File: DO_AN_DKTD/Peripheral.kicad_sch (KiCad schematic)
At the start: 92 parts, among them IC1 RTC_DS3231M, J1 Conn_01x03, J2 Conn_01x02, J4 Conn_01x04, J5 Conn_01x02, J8 Micro_SD_Card_Det1, J9 USB_C_Receptacle, Q1 NPN, Q2 NPN, Q3 NPN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

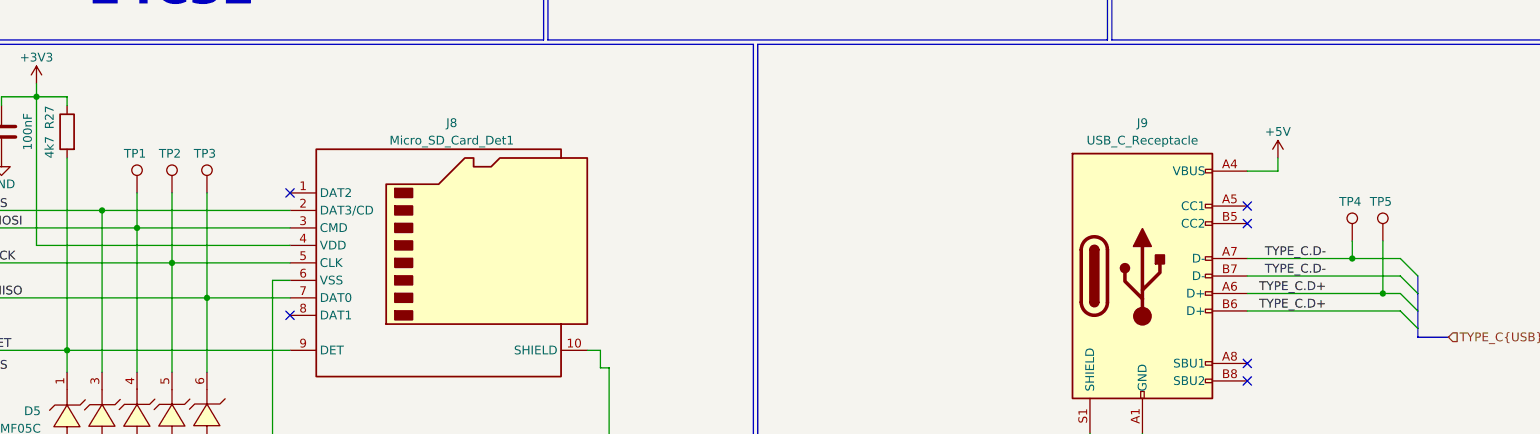
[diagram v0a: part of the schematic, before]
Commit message: add testoint SPI USB LEDTEST and Buck power
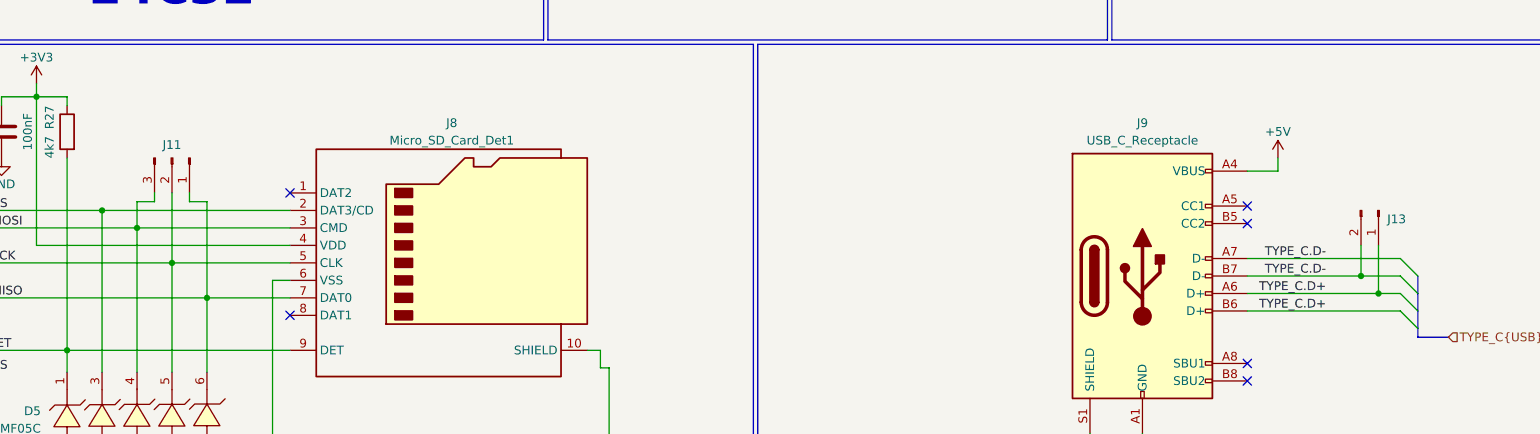
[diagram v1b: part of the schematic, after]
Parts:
- removed TP1, TP2, TP3, TP4, TP5: TestPoint, TestPoint:TestPoint_THTPad_D2.0mm_Drill1.0mm, symbol Connector:TestPoint
- added J11: Conn_01x03_Pin, Connector_PinHeader_2.00mm:PinHeader_1x03_P2.00mm_Vertical, symbol Connector:Conn_01x03_Pin
- added J13: Conn_01x02_Pin, Connector_PinHeader_2.00mm:PinHeader_1x02_P2.00mm_Vertical, symbol Connector:Conn_01x02_Pin
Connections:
- net SD.MISO: now also J11.1 (Pin_1)
- net SD.MOSI: now also J11.3 (Pin_3)
- net SD.SCK: now also J11.2 (Pin_2)
- net TYPE_C.D+: now also J13.1 (Pin_1)
- net TYPE_C.D-: now also J13.2 (Pin_2)

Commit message: commit to change branch
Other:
- note added: "BUZZER"
- note added: "USB TYPE-C"
- moved on the sheet: BZ1, Q9, R27
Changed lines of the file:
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@@
   )
   (bus_alias "pLORA" (members "INT" "CS" "RST"))
-  (bus_alias "SPI" (members "SCK" "MOSI" "MISO"))
   (bus_alias "I2C" (members "SDA" "SCL"))
+  (bus_alias "SPI" (members "SCK" "MOSI" "MISO"))
   (junction (at 258.445 239.395) (diameter 0) (color 0 0 0 0)
   )
@@
   (junction (at 132.715 130.175) (diameter 0) (color 0 0 0 0)
   )
-  (junction (at 376.555 214.63) (diameter 0) (color 0 0 0 0)
+  (junction (at 422.91 238.76) (diameter 0) (color 0 0 0 0)
   )
   (junction (at 247.015 186.055) (diameter 0) (color 0 0 0 0)
@@
   (junction (at 136.525 122.555) (diameter 0) (color 0 0 0 0)
   )
-  (junction (at 367.03 203.835) (diameter 0) (color 0 0 0 0)
+  (junction (at 413.385 227.965) (diameter 0) (color 0 0 0 0)
   )
   (junction (at 347.345 74.295) (diameter 0) (color 0 0 0 0)
@@
     (stroke (width 0) (type default))
   )
+  (polyline (pts (xy 354.33 176.53) (xy 354.33 281.305))
+    (stroke (width 0) (type default))
+  )
   (polyline (pts (xy 354.33 95.25) (xy 486.41 95.25))
     (stroke (width 0) (type default))
@@
     (stroke (width 0) (type default))
   )
-  (wire (pts (xy 367.03 213.36) (xy 367.03 214.63))
+  (wire (pts (xy 413.385 237.49) (xy 413.385 238.76))
     (stroke (width 0) (type default))
   )
@@
     (stroke (width 0) (type default))
   )
+  (polyline (pts (xy 354.33 176.53) (xy 486.41 176.53))
+    (stroke (width 0) (type default))
+  )
   (polyline (pts (xy 217.17 95.25) (xy 353.695 95.25))
     (stroke (width 0) (type default))
@@
     (stroke (width 0) (type default))
   )
+  (polyline (pts (xy 486.41 176.53) (xy 486.41 281.305))
+    (stroke (width 0) (type default))
+  )
   (bus (pts (xy 123.825 60.96) (xy 131.445 60.96))
     (stroke (width 0) (type default))
@@
     (stroke (width 0) (type default))
   )
-  (wire (pts (xy 364.49 203.835) (xy 367.03 203.835))
+  (wire (pts (xy 410.845 227.965) (xy 413.385 227.965))
     (stroke (width 0) (type default))
   )
@@
     (stroke (width 0) (type default))
   )
-  (wire (pts (xy 377.19 194.945) (xy 376.555 194.945))
+  (wire (pts (xy 423.545 219.075) (xy 422.91 219.075))
     (stroke (width 0) (type default))
   )
@@
     (stroke (width 0) (type default))
   )
-  (wire (pts (xy 367.03 205.74) (xy 367.03 203.835))
+  (wire (pts (xy 413.385 229.87) (xy 413.385 227.965))
     (stroke (width 0) (type default))
   )
@@
     (stroke (width 0) (type default))
   )
-  (wire (pts (xy 367.03 214.63) (xy 376.555 214.63))
+  (wire (pts (xy 413.385 238.76) (xy 422.91 238.76))
     (stroke (width 0) (type default))
   )
@@
     (stroke (width 0) (type default))
   )
-  (wire (pts (xy 367.03 203.835) (xy 368.935 203.835))
+  (wire (pts (xy 413.385 227.965) (xy 415.29 227.965))
     (stroke (width 0) (type default))
   )
@@
     (stroke (width 0) (type default))
   )
-  (wire (pts (xy 377.19 189.865) (xy 376.555 189.865))
+  (wire (pts (xy 423.545 213.995) (xy 422.91 213.995))
     (stroke (width 0) (type default))
   )
@@
     (stroke (width 0) (type default))
   )
-  (wire (pts (xy 376.555 208.915) (xy 376.555 214.63))
+  (wire (pts (xy 422.91 233.045) (xy 422.91 238.76))
     (stroke (width 0) (type default))
   )
@@
     (stroke (width 0) (type default))
   )
-  (wire (pts (xy 376.555 194.945) (xy 376.555 198.755))
+  (wire (pts (xy 422.91 219.075) (xy 422.91 222.885))
     (stroke (width 0) (type default))
   )
@@
     (stroke (width 0) (type default))
   )
-  (wire (pts (xy 376.555 214.63) (xy 376.555 217.17))
+  (wire (pts (xy 422.91 238.76) (xy 422.91 241.3))
     (stroke (width 0) (type default))
   )
@@
     (stroke (width 0) (type default))
   )
+  (polyline (pts (xy 486.41 281.305) (xy 354.33 281.305))
+    (stroke (width 0) (type default))
+  )
   (wire (pts (xy 210.185 130.175) (xy 210.185 162.56))
     (stroke (width 0) (type default))
@@
     (stroke (width 0) (type default))
   )
-  (wire (pts (xy 376.555 186.055) (xy 376.555 189.865))
+  (wire (pts (xy 422.91 210.185) (xy 422.91 213.995))
     (stroke (width 0) (type default))
   )
@@
     (effects (font (size 5 5) bold) (justify left bottom))
   )
+  (text "USB TYPE-C" (at 397.51 172.72 0)
+    (effects (font (size 5 5) bold) (justify left bottom))
+  )
   (text "TRIAC" (at 274.955 277.495 0)
     (effects (font (size 5 5) bold) (justify left bottom))
@@
     (effects (font (size 5 5) bold) (justify left bottom))
   )
+  (text "BUZZER" (at 401.955 275.59 0)
+    (effects (font (size 5 5) bold) (justify left bottom))
+  )
   (label "TYPE_C.D+" (at 436.88 131.445 180) (fields_autoplaced)
     (effects (font (size 1.27 1.27)) (justify right bottom))
@@
     (effects (font (size 1.27 1.27)) (justify right))
   )
-  (hierarchical_label "Buzzer" (shape input) (at 364.49 203.835 180) (fields_autoplaced)
+  (hierarchical_label "Buzzer" (shape input) (at 410.845 227.965 180) (fields_autoplaced)
     (effects (font (size 1.27 1.27)) (justify right))
   )
@@
     )
   )
-  (symbol (lib_id "IVS_SYMBOLS:N_Mosfet") (at 376.555 203.835 0) (unit 1)
+  (symbol (lib_id "IVS_SYMBOLS:N_Mosfet") (at 422.91 227.965 0) (unit 1)
     (in_bom yes) (on_board yes) (dnp no) (fields_autoplaced)
-    (property "Reference" "Q9" (at 380.365 204.47 0)
+    (property "Reference" "Q9" (at 426.72 228.6 0)
       (effects (font (size 1.27 1.27)) (justify left))
     )
-    (property "Value" "N_Mosfet" (at 377.825 217.805 0)
+    (property "Value" "N_Mosfet" (at 424.18 241.935 0)
       (effects (font (size 1.27 1.27)) hide)
     )
-    (property "Footprint" "IVS_FOOTPRINTS:SOT23-3" (at 375.285 224.155 0)
+    (property "Footprint" "IVS_FOOTPRINTS:SOT23-3" (at 421.64 248.285 0)
       (effects (font (size 1.27 1.27)) hide)
     )
-    (property "Datasheet" "https://www.onsemi.com/pub/Collateral/BSS138-D.PDF" (at 380.365 226.695 0)
+    (property "Datasheet" "https://www.onsemi.com/pub/Collateral/BSS138-D.PDF" (at 426.72 250.825 0)
       (effects (font (size 1.27 1.27)) hide)
     )
@@
     )
   )
-  (symbol (lib_id "Device:Buzzer") (at 379.73 192.405 0) (unit 1)
+  (symbol (lib_id "Device:Buzzer") (at 426.085 216.535 0) (unit 1)
     (in_bom yes) (on_board yes) (dnp no) (fields_autoplaced)
-    (property "Reference" "BZ1" (at 384.175 191.77 0)
+    (property "Reference" "BZ1" (at 430.53 215.9 0)
       (effects (font (size 1.27 1.27)) (justify left))
     )
-    (property "Value" "Buzzer" (at 384.175 194.31 0)
+    (property "Value" "Buzzer" (at 430.53 218.44 0)
       (effects (font (size 1.27 1.27)) (justify left))
     )
-    (property "Footprint" "Buzzer_Beeper:Buzzer_12x9.5RM7.6" (at 379.095 189.865 90)
+    (property "Footprint" "Buzzer_Beeper:Buzzer_12x9.5RM7.6" (at 425.45 213.995 90)
       (effects (font (size 1.27 1.27)) hide)
     )
-    (property "Datasheet" "~" (at 379.095 189.865 90)
+    (property "Datasheet" "~" (at 425.45 213.995 90)
       (effects (font (size 1.27 1.27)) hide)
     )
@@
     )
   )
-  (symbol (lib_id "Device:R") (at 367.03 209.55 0) (mirror y) (unit 1)
+  (symbol (lib_id "Device:R") (at 413.385 233.68 0) (mirror y) (unit 1)
     (in_bom yes) (on_board yes) (dnp no)
-    (property "Reference" "R27" (at 364.49 205.74 90)
+    (property "Reference" "R27" (at 410.845 229.87 90)
       (effects (font (size 1.27 1.27)) (justify right))
     )
-    (property "Value" "1M" (at 364.49 210.185 90)
+    (property "Value" "1M" (at 410.845 234.315 90)
       (effects (font (size 1.27 1.27)) (justify right))
     )
-    (property "Footprint" "IVS_FOOTPRINTS:R_0603" (at 368.808 209.55 90)
+    (property "Footprint" "IVS_FOOTPRINTS:R_0603" (at 415.163 233.68 90)
       (effects (font (size 1.27 1.27)) hide)
     )
-    (property "Datasheet" "~" (at 367.03 209.55 0)
+    (property "Datasheet" "~" (at 413.385 233.68 0)
       (effects (font (size 1.27 1.27)) hide)
     )
@@
     )
   )
-  (symbol (lib_name "GND_4") (lib_id "power:GND") (at 376.555 217.17 0) (unit 1)
+  (symbol (lib_name "GND_4") (lib_id "power:GND") (at 422.91 241.3 0) (unit 1)
     (in_bom yes) (on_board yes) (dnp no) (fields_autoplaced)
-    (property "Reference" "#PWR013" (at 376.555 223.52 0)
+    (property "Reference" "#PWR013" (at 422.91 247.65 0)
       (effects (font (size 1.27 1.27)) hide)
     )
-    (property "Value" "GND" (at 376.555 221.615 0)
+    (property "Value" "GND" (at 422.91 245.745 0)
       (effects (font (size 1.27 1.27)))
     )
-    (property "Footprint" "" (at 376.555 217.17 0)
+    (property "Footprint" "" (at 422.91 241.3 0)
       (effects (font (size 1.27 1.27)) hide)
     )
-    (property "Datasheet" "" (at 376.555 217.17 0)
+    (property "Datasheet" "" (at 422.91 241.3 0)
       (effects (font (size 1.27 1.27)) hide)
     )
@@
     )
   )
-  (symbol (lib_id "power:+5V") (at 376.555 186.055 0) (unit 1)
+  (symbol (lib_id "power:+5V") (at 422.91 210.185 0) (unit 1)
     (in_bom yes) (on_board yes) (dnp no) (fields_autoplaced)
-    (property "Reference" "#PWR030" (at 376.555 189.865 0)
+    (property "Reference" "#PWR030" (at 422.91 213.995 0)
       (effects (font (size 1.27 1.27)) hide)
     )
-    (property "Value" "+5V" (at 376.555 182.88 0)
+    (property "Value" "+5V" (at 422.91 207.01 0)
       (effects (font (size 1.27 1.27)))
     )
-    (property "Footprint" "" (at 376.555 186.055 0)
+    (property "Footprint" "" (at 422.91 210.185 0)
       (effects (font (size 1.27 1.27)) hide)
     )
-    (property "Datasheet" "" (at 376.555 186.055 0)
+    (property "Datasheet" "" (at 422.91 210.185 0)
       (effects (font (size 1.27 1.27)) hide)
     )

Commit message: complete code DO_AN_MON
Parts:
- D5: Buy (none) -> https://www.thegioiic.com/smf05c-tct; Supplier and ref (none) -> https://www.thegioiic.com/smf05c-tct
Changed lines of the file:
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@@
     (company "NGUYỄN TRUNG THẢO")
   )
+  (bus_alias "SPI" (members "SCK" "MOSI" "MISO"))
   (bus_alias "I2C" (members "SDA" "SCL"))
   (bus_alias "pLORA" (members "INT" "CS" "RST"))
-  (bus_alias "SPI" (members "SCK" "MOSI" "MISO"))
   (junction (at 258.445 239.395) (diameter 0) (color 0 0 0 0)
   )
@@
       (effects (font (size 1.27 1.27)) hide)
     )
+    (property "Buy" "https://www.thegioiic.com/smf05c-tct" (at 259.461 161.036 0)
+      (effects (font (size 1.27 1.27)) hide)
+    )
+    (property "Supplier and ref" "https://www.thegioiic.com/smf05c-tct" (at 260.604 161.544 0)
+      (effects (font (size 1.27 1.27)) hide)
+    )
